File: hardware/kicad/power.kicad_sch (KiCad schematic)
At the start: 21 parts, among them Q2 FS8205A, U1 TC4056A, U2 DW01A, U3 AP2112K-3.3, U9 MT3608

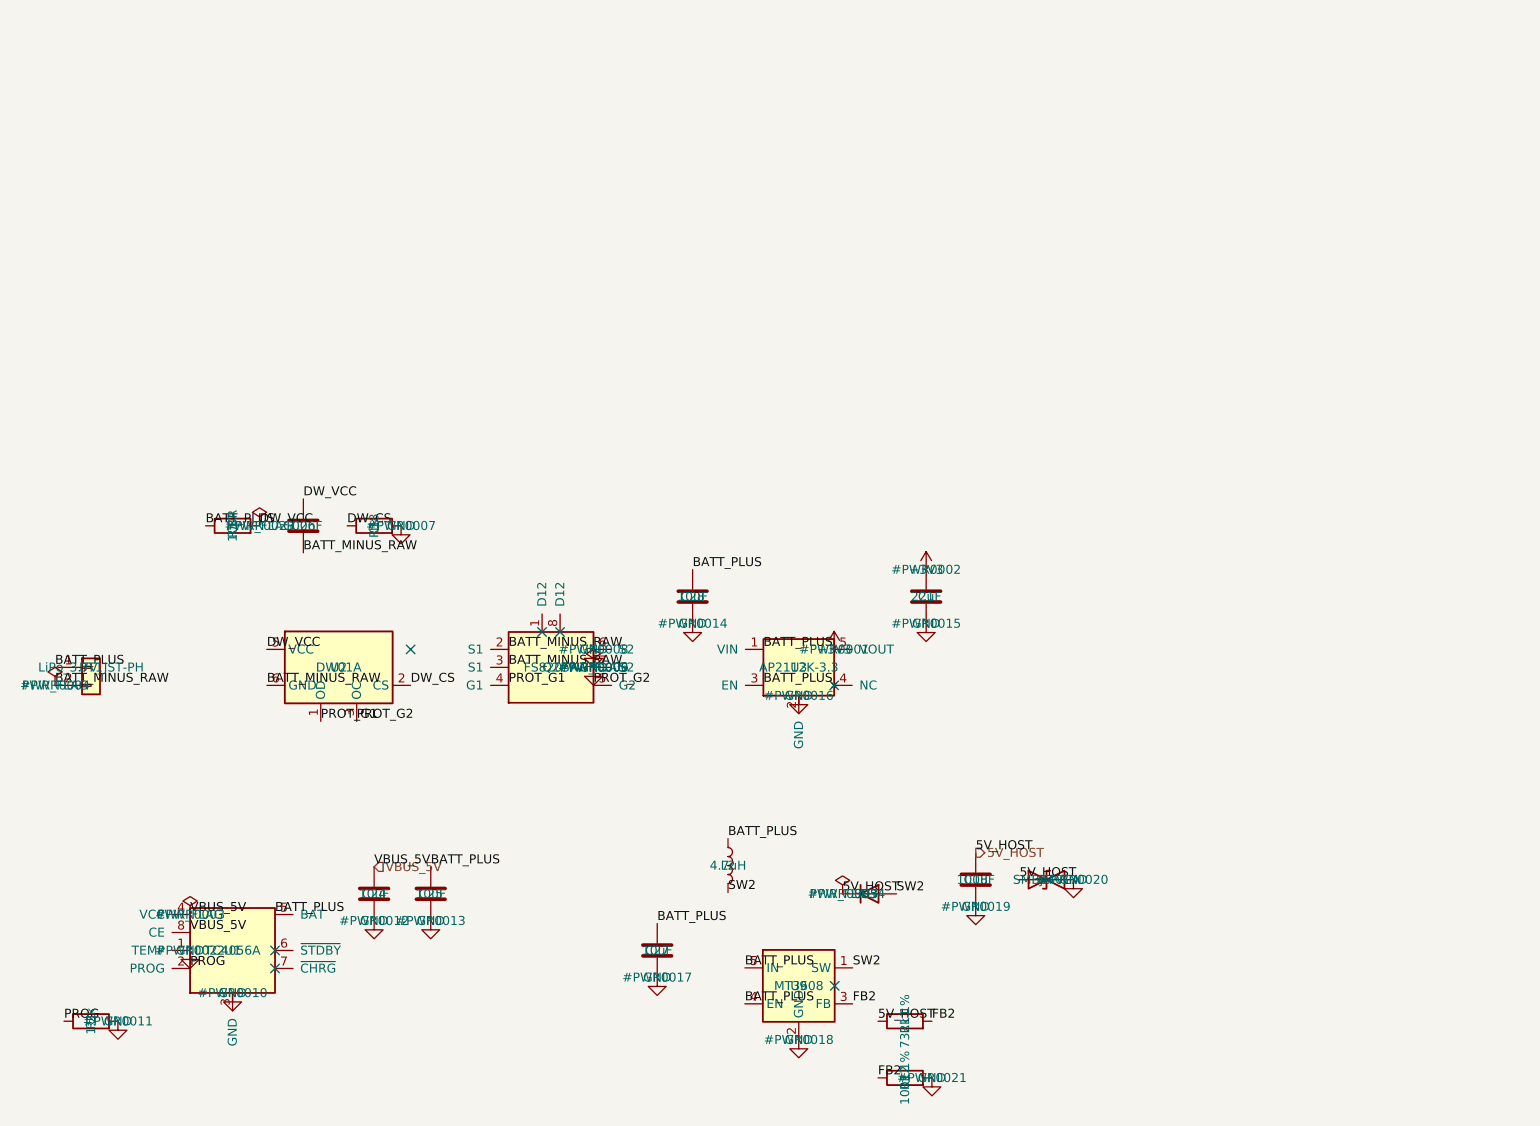
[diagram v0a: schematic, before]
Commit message: Refactored the power schematic.
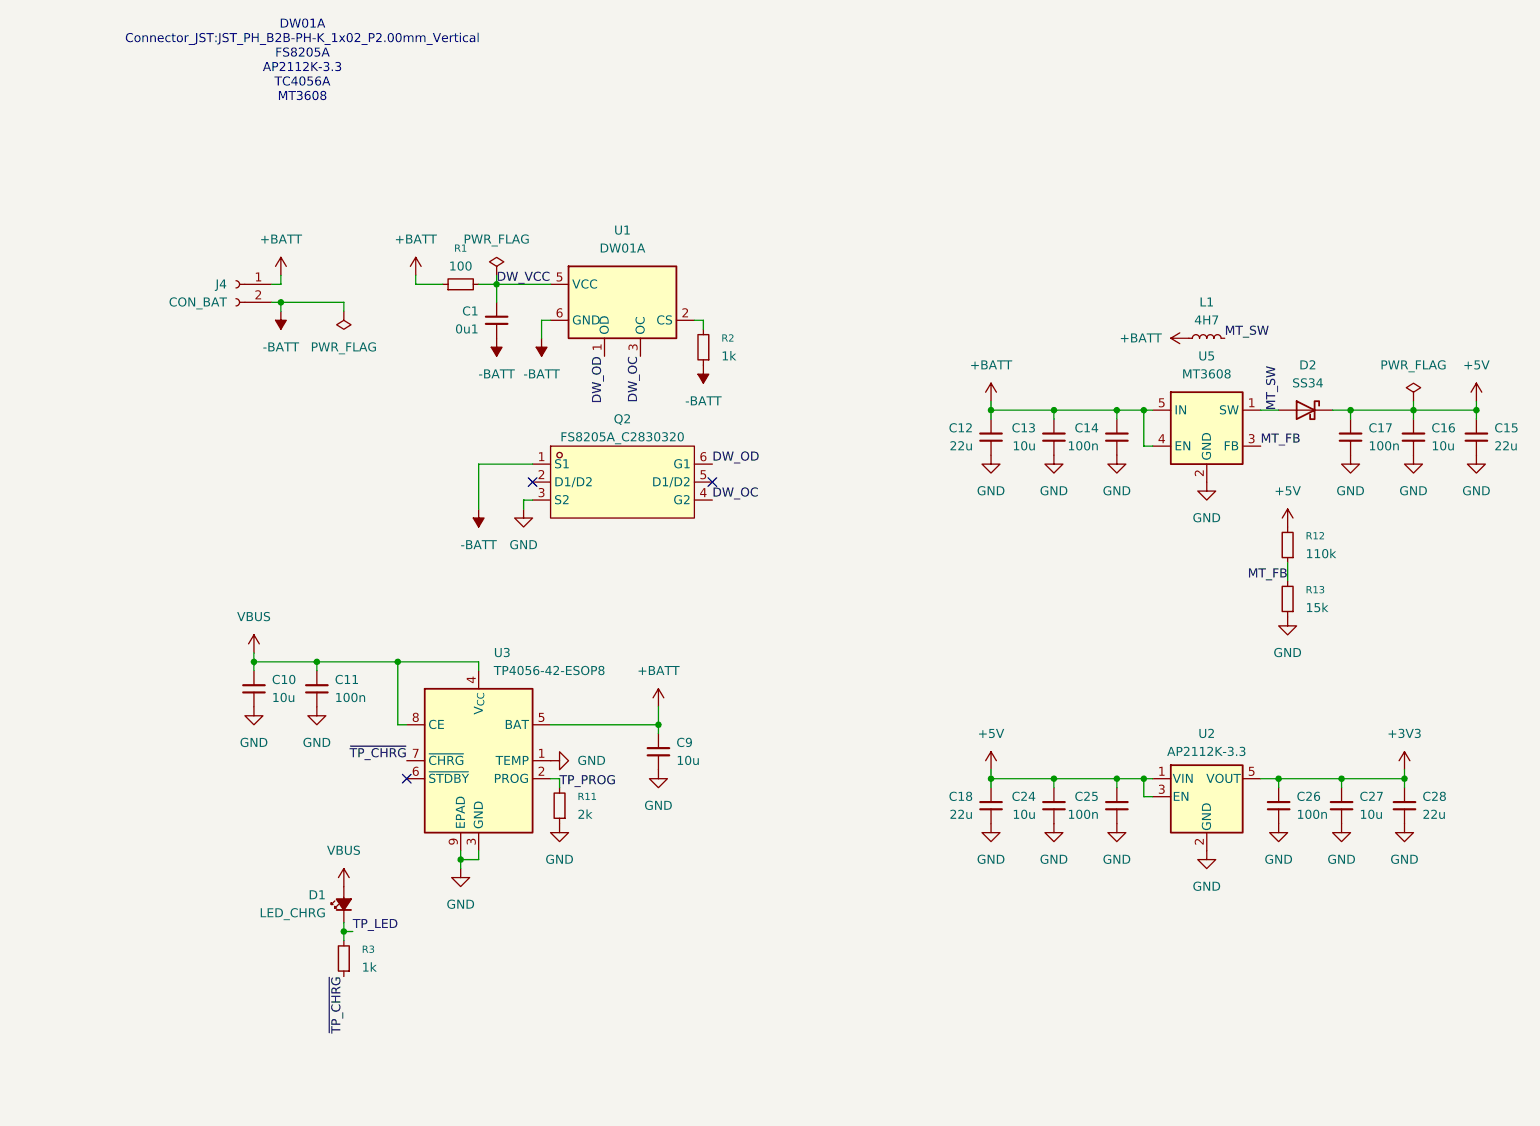
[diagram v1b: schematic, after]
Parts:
- removed BT1: LiPo_3.7V_JST-PH, Connector_JST:JST_PH_B2B-PH-K_1x02_P2.00mm_Vertical, symbol Connector_Generic:Conn_01x02
- removed C1: 22uF, Capacitor_SMD:C_0805_2012Metric, symbol Device:C
- removed C18: 100uF, Capacitor_SMD:C_1206_3216Metric, symbol Device:C
- removed C24, C25, C27, C28: 10uF, Capacitor_SMD:C_0805_2012Metric, symbol Device:C
- removed C26: 100nF, Capacitor_SMD:C_0603_1608Metric, symbol Device:C
- removed D3: SS34, Diode_SMD:D_SMA, symbol Device:D
- removed D4: SMBJ5.0CA, Diode_SMD:D_SMB, symbol Device:D_TVS
- removed L2: 4.7uH, Inductor_SMD:L_6.3x6.3_H3, symbol Device:L
- removed Q2: FS8205A, Package_SO:TSSOP-8_4.4x3mm_P0.65mm, symbol WaveRig_Custom:FS8205A_TSSOP8
- removed R1: 1.2k, Resistor_SMD:R_0603_1608Metric, symbol Device:R
- removed R11: 732k 1%, Resistor_SMD:R_0603_1608Metric, symbol Device:R
- removed R12: 100k 1%, Resistor_SMD:R_0603_1608Metric, symbol Device:R
- removed R17: 100R, Resistor_SMD:R_0603_1608Metric, symbol Device:R
- removed R18: 1k, Resistor_SMD:R_0603_1608Metric, symbol Device:R
- removed U1: TC4056A, Package_SO:SOIC-8_3.9x4.9mm_P1.27mm, symbol WaveRig_Custom:TC4056A_SOP8
- removed U2: DW01A, Package_TO_SOT_SMD:SOT-23-6, symbol Battery_Management:DW01A
- removed U3: AP2112K-3.3, Package_TO_SOT_SMD:SOT-23-5, symbol WaveRig_Custom:AP2112K-3.3
- removed U9: MT3608, Package_TO_SOT_SMD:SOT-23-6, symbol Regulator_Switching:MT3608
- added C1: 0u1, Capacitor_SMD:C_0603_1608Metric, symbol Device:C_Small
- added C10, C13, C16, C24, C27, C9: 10u, Capacitor_SMD:C_0603_1608Metric, symbol Device:C_Small
- added C11, C14, C17, C25, C26: 100n, Capacitor_SMD:C_0603_1608Metric, symbol Device:C_Small
- added C12, C15, C18, C28: 22u, Capacitor_SMD:C_0603_1608Metric, symbol Device:C_Small
- added D1: LED_CHRG, LED_SMD:LED_0603_1608Metric, symbol Device:LED_Small_Filled
- added D2: SS34, Diode_SMD:D_SMA, symbol Diode:SS34
- added J4: CON_BAT, Connector_JST:JST_PH_B2B-PH-K_1x02_P2.00mm_Vertical, symbol Connector:Conn_01x02_Socket
- added L1: 4H7, Inductor_SMD:L_APV_APH0530, symbol Device:L_Small
- added Q2: FS8205A_C2830320, WaveRig_Custom:SOT-23-6_L2.9-W1.6-P0.95-LS2.8-BR, symbol WaveRig_Custom:FS8205A_C2830320
- added R1: 100, Resistor_SMD:R_0603_1608Metric, symbol Device:R_Small
- added R11: 2k, Resistor_SMD:R_0603_1608Metric, symbol Device:R_Small
- added R12: 110k, Resistor_SMD:R_0603_1608Metric, symbol Device:R_Small
- added R13: 15k, Resistor_SMD:R_0603_1608Metric, symbol Device:R_Small
- added R2, R3: 1k, Resistor_SMD:R_0603_1608Metric, symbol Device:R_Small
- added U1: DW01A, Package_TO_SOT_SMD:SOT-23-6, symbol Battery_Management:DW01A
- added U2: AP2112K-3.3, Package_TO_SOT_SMD:SOT-23-5, symbol Regulator_Linear:AP2112K-3.3
- added U3: TP4056-42-ESOP8, Package_SO:SOIC-8-1EP_3.9x4.9mm_P1.27mm_EP2.41x3.3mm_ThermalVias, symbol Battery_Management:TP4056-42-ESOP8
- added U5: MT3608, Package_TO_SOT_SMD:SOT-23-6, symbol Regulator_Switching:MT3608
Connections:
- net +3V3: now also C26.1, C27.1, C28.1, U2.5 (VOUT)
- net DW_VCC: now also C1.1, R1.2, U1.5 (VCC)
- net GND: now also C10.2, C11.2, C12.2, C13.2, C14.2, C15.2, C16.2, C17.2, C18.2, C24.2, C25.2, C26.2, C27.2, C28.2, C9.2, Q2.3 (S2), R11.1, R13.1, U2.2 (GND), U3.1 (TEMP), U3.3 (GND), U3.9 (EPAD), U5.2 (GND)
- new net: R2.2, U1.2 (CS)
- new net +5V: C15.1, C16.1, C17.1, C18.1, C24.1, C25.1, D2.1 (K), R12.2, U2.1 (VIN), U2.3 (EN)
- new net +BATT: C12.1, C13.1, C14.1, C9.1, J4.1 (Pin_1), L1.1, R1.1, U3.5 (BAT), U5.4 (EN), U5.5 (IN)
- new net -BATT: C1.2, J4.2 (Pin_2), Q2.1 (S1), R2.1, U1.6 (GND)
- new net DW_OC: Q2.4 (G2), U1.3 (OC)
- new net DW_OD: Q2.6 (G1), U1.1 (OD)
- new net MT_FB: R12.1, R13.2, U5.3 (FB)
- new net MT_SW: D2.2 (A), L1.2, U5.1 (SW)
- new net TP_LED: D1.1 (K), R3.2
- new net TP_PROG: R11.2, U3.2 (PROG)
- new net VBUS: C10.1, C11.1, D1.2 (A), U3.4 (V_{CC}), U3.8 (CE)
- new net ~{TP_CHRG}: R3.1, U3.7 (~{CHRG})
- no-connect marks 7 -> 3
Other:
- note added: "DW01A Connector_JST:JST_PH_B2B-PH-K_1x02_P2.00mm_Vertical FS8205A AP2112K-3.3 TC4056A MT3608"

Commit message: Refactor the microcontroller sheet; add switch footprint and 3d file; add titles, date and WaveRig annotation to all sheets.
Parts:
- C1: value 0u1 -> 100n
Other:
- company: (none) -> WaveRig
- title: (none) -> Power Management
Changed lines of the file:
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@@
 	(generator_version "10.0")
 	(paper "A4")
+	(title_block
+		(title "Power Management")
+		(date "2026-09-25")
+		(rev "0.1")
+		(company "WaveRig")
+	)
 	(text "DW01A\nConnector_JST:JST_PH_B2B-PH-K_1x02_P2.00mm_Vertical\nFS8205A\nAP2112K-3.3\nTC4056A\nMT3608"
 		(exclude_from_sim no)
@@
 			)
 		)
-		(property "Value" "0u1"
+		(property "Value" "100n"
 			(at 64.77 62.2299 0)
 			(show_name no)
